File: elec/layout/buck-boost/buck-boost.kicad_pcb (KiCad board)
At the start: 2 copper layers, 62 parts, among them U10 2.49kΩ ±1% 100mW, U11 4.7µF ±10% 100V X7R, U12 4.7µF ±10% 100V X7R, U13 4.7µF ±10% 100V X7R, U14 10µF ±10% 100V X7R, U15 10µF ±10% 100V X7R, U16 10µF ±10% 100V X7R, U17 10µF ±10% 100V X7R, U18 1µF ±10% 100V X7R, U19 100nF ±10% 100V X7R, U2 100nF ±10% 50V X7R, U20 100pF ±5% 100V C0G, U21 470nF ±20% 16V X5R, U22 100nF ±10% 16V X7R, U23 10Ω ±1% 62.5mW, U24 100nF ±10% 16V X7R, U25 10Ω ±1% 62.5mW, U26 5mΩ ±1% 1W, U27 4.7µF ±10% 100V X7R, U28 4.7µF ±10% 100V X7R, U29 4.7µF ±10% 100V X7R, U3 100nF ±10% 50V X7R, U30 10µF ±10% 100V X7R, U31 10µF ±10% 100V X7R, U32 10µF ±10% 100V X7R, U33 10µF ±10% 100V X7R, U34 1µF ±10% 100V X7R, U35 100nF ±10% 100V X7R, U36 100pF ±5% 100V C0G, U37 470nF ±20% 16V X5R, U38 100nF ±10% 16V X7R, U39 10Ω ±1% 62.5mW, U4 0Ω 100mW, U40 100nF ±10% 16V X7R, U41 10Ω ±1% 62.5mW, U42 5mΩ ±1% 1W, U43 13.7kΩ ±1% 62.5mW, U44 249kΩ ±1% 62.5mW, U45 1MΩ ±1% 250mW, U46 133kΩ ±1% 62.5mW, U47 25.5kΩ ±1% 62.5mW, U48 4.7µF ±10% 25V X5R, U49 100nF ±10% 100V X7R, U5 0Ω 100mW, U50 1µF ±10% 100V X7R, U51 4.7µF ±10% 100V X7R, U52 4.7µF ±10% 100V X7R, U6 0Ω 100mW, U7 0Ω 100mW, U9 4.7µF ±10% 25V X5R

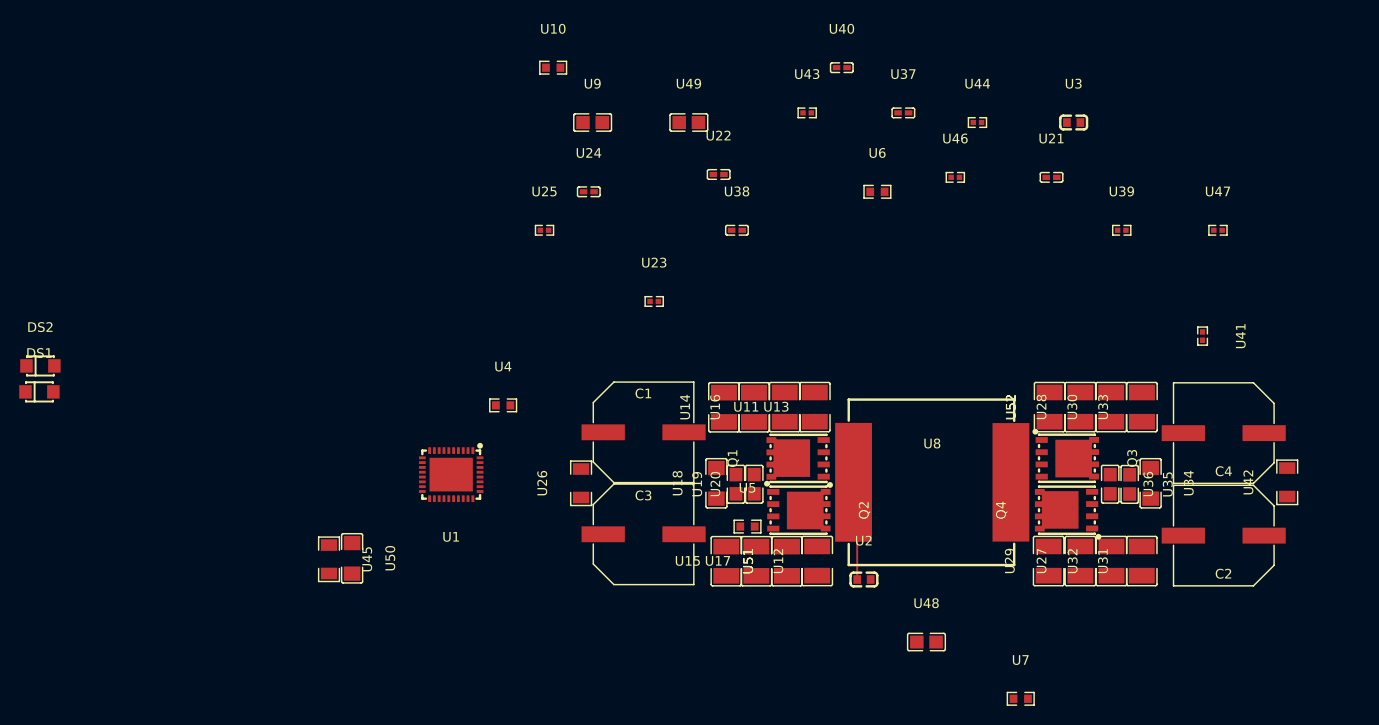
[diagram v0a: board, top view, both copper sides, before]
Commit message: update buck boost
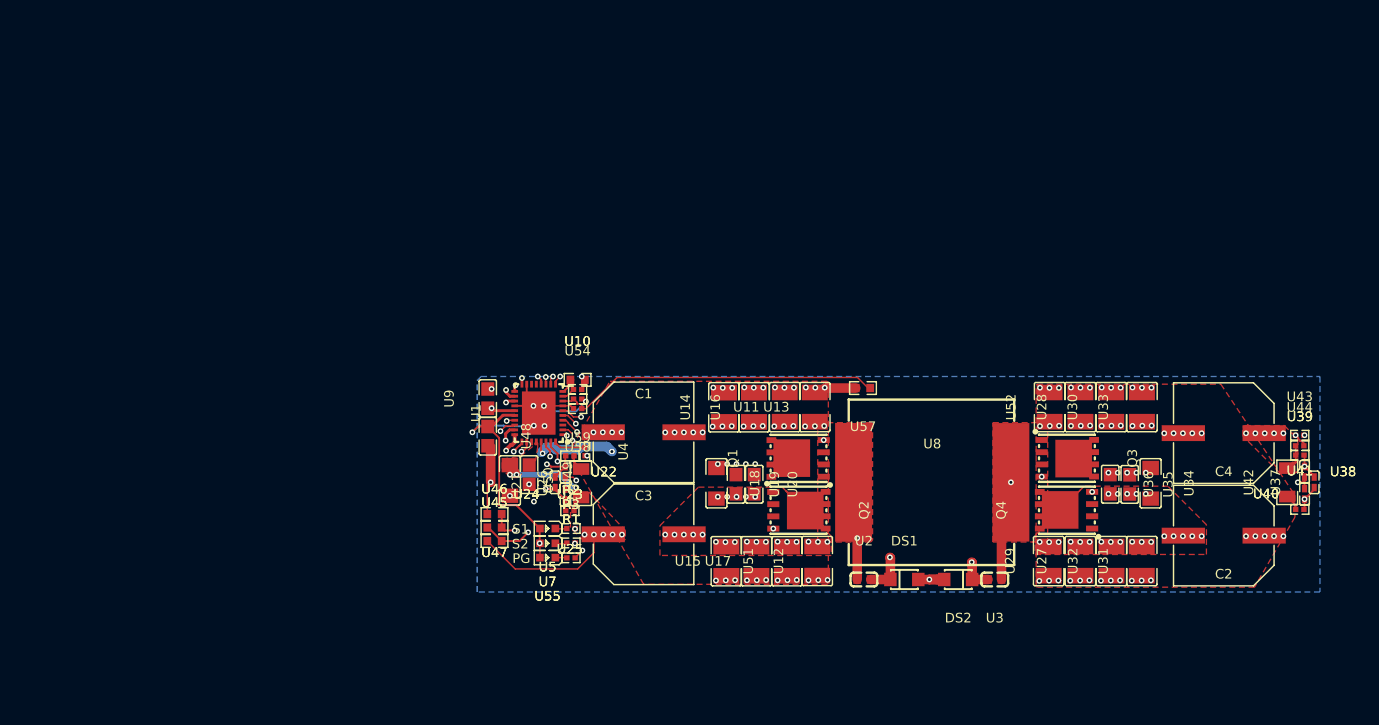
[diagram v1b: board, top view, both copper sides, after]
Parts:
- removed U6: 0Ω 100mW, atopile:R0603-ebcab9
- added R1: 100Ω ±1% 62.5mW, atopile:R0402-56259e, F.Cu at (135.3, 77.2)
- added R2: 100Ω ±1% 62.5mW, atopile:R0402-56259e, F.Cu at (135.3, 74.2)
- added R3: 100Ω ±1% 62.5mW, atopile:R0402-56259e, F.Cu at (135.3, 75.7)
- added U54: 0Ω 62.5mW, atopile:R0402-56259e, F.Cu at (136.0, 59.7)
- added U55: , atopile:LED0603-RD-c81ffb, F.Cu at (132.9, 77.2)
- added U57: , atopile:R0603-ebcab9, F.Cu at (165.7, 59.6)
- added U58: 30.1kΩ ±1% 62.5mW, atopile:R0402-56259e, F.Cu at (136.0, 61.7)
- added U59: 5.23kΩ ±1% 62.5mW, atopile:R0402-56259e, F.Cu at (136.0, 60.7)
- U4: value 0Ω 100mW -> 50kΩ ±1% 62.5mW; footprint atopile:R0603-ebcab9 -> atopile:R0402-56259e
- U45: value 1MΩ ±1% 250mW -> 1MΩ ±1% 100mW; footprint atopile:R1206-bdb864 -> atopile:R0603-ebcab9
- U46: value 133kΩ ±1% 62.5mW -> 133kΩ ±1% 100mW; footprint atopile:R0402-56259e -> atopile:R0603-ebcab9
- U47: value 25.5kΩ ±1% 62.5mW -> 25.5kΩ ±0% 100mW; footprint atopile:R0402-56259e -> atopile:R0603-ebcab9
- U5, U7: value 0Ω 100mW -> (none); footprint atopile:R0603-ebcab9 -> atopile:LED0603-RD-c81ffb
- moved DS2 97.9 mm to (175.6, 79.5), turned to 180 degrees
- moved DS1 92.0 mm to (170.0, 79.5)
- moved U47 80.8 mm to (127.4, 72.7), turned to 180 degrees
- moved U40 65.4 mm to (211.6, 70.6), turned to 90 degrees
- moved U38 64.1 mm to (211.6, 68.3), turned to -90 degrees
- moved U43 61.2 mm to (211.1, 64.5)
- moved U21 60.6 mm to (133.7, 69.4), turned to 90 degrees
- moved U46 60.2 mm to (127.4, 74.1)
- moved U37 57.4 mm to (212.6, 69.4), turned to 90 degrees
- moved U7 51.8 mm to (132.9, 75.7), turned to 180 degrees
- moved U48 50.4 mm to (126.7, 64.6), turned to -90 degrees
- moved U3 48.2 mm to (179.4, 79.5), turned to 180 degrees
- moved U44 47.4 mm to (211.1, 65.6)
- moved U49 40.2 mm to (131.0, 68.6), turned to -90 degrees
- moved U22 34.8 mm to (134.8, 68.3), turned to -90 degrees
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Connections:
- net out renamed FB
- C1 pad 1: hv-1 -> hv-2
- C1 pad 2: gnd -> gnd-3
- C2 pad 2: core.output_cap-net -> gnd-3
- C3 pad 2: gnd -> gnd-3
- C4 pad 1: hv-2 -> hv-1
- C4 pad 2: output_electrolytic-net -> gnd-3
- DS1 pad 1: bst_diode_input.footprint.pins[0].net-net -> cathode-1
- DS1 pad 2: bst_diode_input.footprint.pins[1].net-net -> anode
- DS2 pad 1: bst_diode_output.footprint.pins[0].net-net -> cathode
- DS2 pad 2: bst_diode_output.footprint.pins[1].net-net -> anode
- Q1 pad 1: input_switching_node -> SW1
- Q1 pad 2: input_switching_node -> SW1
- Q1 pad 3: input_switching_node -> SW1
- Q1 pad 4: core-gate-2 -> line-4
- Q1 pad 5: hv-1 -> hv-2
- Q1 pad 6: hv-1 -> hv-2
- Q1 pad 7: hv-1 -> hv-2
- Q1 pad 8: hv-1 -> hv-2
- Q2 pad 1: gnd -> gnd-3
- Q2 pad 2: gnd -> gnd-3
- Q2 pad 3: gnd -> gnd-3
- Q2 pad 4: core-gate -> line-3
- Q2 pad 5: input_switching_node -> SW1
- Q2 pad 6: input_switching_node -> SW1
- Q2 pad 7: input_switching_node -> SW1
- Q2 pad 8: input_switching_node -> SW1
- Q3 pad 1: output_switching_node -> SW2
- Q3 pad 2: output_switching_node -> SW2
- Q3 pad 3: output_switching_node -> SW2
- Q3 pad 4: core-gate-3 -> line
- Q4 pad 1: gnd -> gnd-3
- Q4 pad 2: gnd -> gnd-3
- Q4 pad 3: gnd -> gnd-3
- Q4 pad 4: core-gate-1 -> line-2
- Q4 pad 5: output_switching_node -> SW2
- Q4 pad 6: output_switching_node -> SW2
- Q4 pad 7: output_switching_node -> SW2
- Q4 pad 8: output_switching_node -> SW2
- U1 pad 13: SRN -> output_shunt.diff_cap-net-1
- U1 pad 14: SRP -> output_shunt.diff_cap-net
- U1 pad 17: gnd -> gnd-3
- U1 pad 19: gate_output_hs -> line
- U1 pad 20: anode -> cathode
- U1 pad 21: gate_output_ls -> line-2
- U1 pad 22: gnd -> gnd-3
- U1 pad 24: REGN -> anode-1
- U1 pad 25: gate_input_ls -> line-3
- U1 pad 26: bst_input -> cathode-1
- U1 pad 27: gate_input_hs -> line-4
- U1 pad 29: ACN -> line-7
- U1 pad 30: ACP -> line-5
- U1 pad 33: hv-2 -> hv-1
- U1 pad 37: gnd -> gnd-3
- U1 pad 4: STAT1 -> gnd
- U1 pad 5: STAT2 -> gnd-4
- U1 pad 6: PGh -> gnd-5
- U1 pad 7: CEh -> gnd-3
- U10 pad 2: gnd -> gnd-3
- U11 pad 1: hv-1 -> hv-2
- U11 pad 2: gnd -> gnd-3
- U12 pad 1: hv-1 -> hv-2
- U12 pad 2: gnd -> gnd-3
- U13 pad 1: hv-1 -> hv-2
- U13 pad 2: gnd -> gnd-3
- U14 pad 1: hv-1 -> hv-2
- U14 pad 2: gnd -> gnd-3
- U15 pad 1: hv-1 -> hv-2
- U15 pad 2: gnd -> gnd-3
- U16 pad 1: hv-1 -> hv-2
- U16 pad 2: gnd -> gnd-3
- U17 pad 1: hv-1 -> hv-2
- U17 pad 2: gnd -> gnd-3
- U18 pad 1: hv-1 -> hv-2
- U18 pad 2: gnd -> gnd-3
- U19 pad 1: hv-1 -> hv-2
- U19 pad 2: gnd -> gnd-3
- U2 pad 1: input_switching_node -> SW1
- U2 pad 2: bst_input -> cathode-1
- U20 pad 1: hv-1 -> hv-2
- U20 pad 2: gnd -> gnd-3
- U21 pad 1: input_shunt.diff_cap-net-1 -> line-5
- U21 pad 2: input_shunt.diff_cap-net -> line-7
- U22 pad 1: ACN -> line-7
- U22 pad 2: gnd -> gnd-3
- U23 pad 1: hv-1 -> hv-2
- U23 pad 2: ACN -> line-7
- U24 pad 1: ACP -> line-5
- U24 pad 2: gnd -> gnd-3
- U25 pad 2: ACP -> line-5
- U26 pad 2: hv-1 -> hv-2
- U27 pad 2: gnd -> gnd-3
- U28 pad 2: gnd -> gnd-3
- U29 pad 2: gnd -> gnd-3
- U3 pad 1: output_switching_node -> SW2
- U3 pad 2: anode -> cathode
- U30 pad 2: gnd -> gnd-3
- U31 pad 2: gnd -> gnd-3
- U32 pad 2: gnd -> gnd-3
- U33 pad 2: gnd -> gnd-3
- U34 pad 2: gnd -> gnd-3
- U35 pad 2: gnd -> gnd-3
- U36 pad 2: gnd -> gnd-3
- U37 pad 1: output_shunt.diff_cap-net-1 -> output_shunt.diff_cap-net
- U37 pad 2: output_shunt.diff_cap-net -> output_shunt.diff_cap-net-1
- U38 pad 1: SRN -> output_shunt.diff_cap-net-1
- U38 pad 2: gnd -> gnd-3
- U39 pad 1: hv-2 -> hv-1
- U39 pad 2: SRN -> output_shunt.diff_cap-net-1
- U4 pad 1: gate_input_hs -> FSW_SYNC
- U4 pad 2: core-gate-2 -> gnd-3
- U40 pad 1: SRP -> output_shunt.diff_cap-net
- U40 pad 2: gnd -> gnd-3
- U41 pad 2: SRP -> output_shunt.diff_cap-net
- U42 pad 2: hv-2 -> hv-1
- U44 pad 1: hv-2 -> hv-1
- U47 pad 2: gnd -> gnd-3
- U48 pad 1: REGN -> anode-1
- U48 pad 2: gnd -> gnd-3
- U49 pad 2: gnd -> gnd-3
- U5 pad 1: gate_input_ls -> status_1_led-cathode
- U5 pad 2: core-gate -> anode-1
- U50 pad 2: gnd -> gnd-3
- U51 pad 1: hv-1 -> hv-2
- U51 pad 2: gnd -> gnd-3
- U52 pad 2: gnd -> gnd-3
- U7 pad 1: gate_output_ls -> status_2_led-cathode
- U7 pad 2: core-gate-1 -> anode-1
- U8 pad 1: input_switching_node -> SW1
- U8 pad 2: output_switching_node -> SW2
- U9 pad 2: gnd -> gnd-3
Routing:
- net output_shunt.diff_cap-net: track 0.00 -> 88.9 mm, vias 0 -> 2
- net output_shunt.diff_cap-net-1: track 0.00 -> 86.4 mm, vias 0 -> 2
- net FB: track 0.00 -> 82.8 mm, vias 0 -> 2
- net gnd-1: track 0.00 -> 81.7 mm, vias 0 -> 2
- net hv-1: track 0.00 -> 78.8 mm, vias 0 -> 7
- net anode: track 0.00 -> 70.3 mm, vias 0 -> 2
- net SW2: track 0.00 -> 68.3 mm, vias 0 -> 2
- net line-2: track 0.00 -> 67.3 mm, vias 0 -> 2
- net cathode: track 0.00 -> 62.4 mm, vias 0 -> 2
- net cathode-1: track 0.00 -> 59.5 mm, vias 0 -> 2
- net line: track 0.00 -> 59.3 mm, vias 0 -> 2
- net SW1: track 0.00 -> 55.2 mm, vias 0 -> 3
- net line-3: track 0.00 -> 38.0 mm, vias 0 -> 2
- net line-4: track 0.00 -> 37.8 mm, vias 0 -> 2
- net anode-1: track 0.00 -> 35.4 mm, vias 0 -> 3
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- added copper zone on F.Cu, net SW1
- added copper zone on F.Cu, net SW2
- added copper zone on B.Cu, net gnd-3
- added copper zone on F.Cu, net gnd-3
- added copper zone on In1.Cu, net gnd-3
- added copper zone on F.Cu, net hv
- added copper zone on F.Cu, net hv-1
- added copper zone on F.Cu, net hv-2
- added copper zone on In2.Cu, net hv-2
- added copper zone on F.Cu, net hv-3
- added copper zone on In2.Cu, net hv-3
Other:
- copper layers 2 -> 6
- board text added: "PG"
- board text added: "S1"
- board text added: "S2"

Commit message: Everything builds
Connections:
- net SW1 renamed core-line
- net SW2 renamed source
- net line-2 renamed gate
- net line-4 renamed gate-1
- net line-7 renamed input_shunt.diff_cap-net
- net output_shunt.diff_cap-net renamed line-1
- C1 pad 2: gnd-3 -> gnd-4
- C2 pad 1: hv-3 -> hv
- C2 pad 2: gnd-3 -> gnd-4
- C3 pad 1: hv -> hv-3
- C3 pad 2: gnd-3 -> gnd-4
- C4 pad 2: gnd-3 -> gnd-4
- DS1 pad 1: cathode-1 -> cathode
- DS2 pad 1: cathode -> cathode-1
- Q2 pad 1: gnd-3 -> gnd-4
- Q2 pad 2: gnd-3 -> gnd-4
- Q2 pad 3: gnd-3 -> gnd-4
- Q2 pad 4: line-3 -> gate-2
- Q3 pad 5: hv-3 -> hv
- Q3 pad 6: hv-3 -> hv
- Q3 pad 7: hv-3 -> hv
- Q3 pad 8: hv-3 -> hv
- Q4 pad 1: gnd-3 -> gnd-4
- Q4 pad 2: gnd-3 -> gnd-4
- Q4 pad 3: gnd-3 -> gnd-4
- R1 pad 2: gnd-5 -> gnd-6
- R2 pad 2: gnd -> gnd-1
- R3 pad 2: gnd-4 -> gnd-3
- U1 pad 11: gnd-1 -> gnd-5
- U1 pad 17: gnd-3 -> gnd-4
- U1 pad 20: cathode -> cathode-1
- U1 pad 22: gnd-3 -> gnd-4
- U1 pad 25: line-3 -> gate-2
- U1 pad 26: cathode-1 -> cathode
- U1 pad 30: line-5 -> line-3
- U1 pad 32: hv -> hv-3
- U1 pad 37: gnd-3 -> gnd-4
- U1 pad 4: gnd -> gnd-1
- U1 pad 5: gnd-4 -> gnd-3
- U1 pad 6: gnd-5 -> gnd-6
- U1 pad 7: gnd-3 -> gnd-4
- U10 pad 2: gnd-3 -> gnd-4
- U11 pad 2: gnd-3 -> gnd-4
- U12 pad 2: gnd-3 -> gnd-4
- U13 pad 2: gnd-3 -> gnd-4
- U14 pad 2: gnd-3 -> gnd-4
- U15 pad 2: gnd-3 -> gnd-4
- U16 pad 2: gnd-3 -> gnd-4
- U17 pad 2: gnd-3 -> gnd-4
- U18 pad 2: gnd-3 -> gnd-4
- U19 pad 2: gnd-3 -> gnd-4
- U2 pad 2: cathode-1 -> cathode
- U20 pad 2: gnd-3 -> gnd-4
- U21 pad 1: line-5 -> line-3
- U22 pad 2: gnd-3 -> gnd-4
- U24 pad 1: line-5 -> line-3
- U24 pad 2: gnd-3 -> gnd-4
- U25 pad 1: hv -> hv-3
- U25 pad 2: line-5 -> line-3
- U26 pad 1: hv -> hv-3
- U27 pad 1: hv-3 -> hv
- U27 pad 2: gnd-3 -> gnd-4
- U28 pad 1: hv-3 -> hv
- U28 pad 2: gnd-3 -> gnd-4
- U29 pad 1: hv-3 -> hv
- U29 pad 2: gnd-3 -> gnd-4
- U3 pad 2: cathode -> cathode-1
- U30 pad 1: hv-3 -> hv
- U30 pad 2: gnd-3 -> gnd-4
- U31 pad 1: hv-3 -> hv
- U31 pad 2: gnd-3 -> gnd-4
- U32 pad 1: hv-3 -> hv
- U32 pad 2: gnd-3 -> gnd-4
- U33 pad 1: hv-3 -> hv
- U33 pad 2: gnd-3 -> gnd-4
- U34 pad 1: hv-3 -> hv
- U34 pad 2: gnd-3 -> gnd-4
- U35 pad 1: hv-3 -> hv
- U35 pad 2: gnd-3 -> gnd-4
- U36 pad 1: hv-3 -> hv
- U36 pad 2: gnd-3 -> gnd-4
- U38 pad 2: gnd-3 -> gnd-4
- U4 pad 2: gnd-3 -> gnd-4
- U40 pad 2: gnd-3 -> gnd-4
- U41 pad 1: hv-3 -> hv
- U42 pad 1: hv-3 -> hv
- U43 pad 2: gnd-1 -> gnd-5
- U45 pad 1: hv -> hv-3
- U47 pad 2: gnd-3 -> gnd-4
- U48 pad 2: gnd-3 -> gnd-4
- U49 pad 1: hv -> hv-3
- U49 pad 2: gnd-3 -> gnd-4
- U50 pad 1: hv -> hv-3
- U50 pad 2: gnd-3 -> gnd-4
- U51 pad 2: gnd-3 -> gnd-4
- U52 pad 1: hv-3 -> hv
- U52 pad 2: gnd-3 -> gnd-4
- U54 pad 2: gnd-3 -> gnd-4
- U57 pad 2: gnd-3 -> gnd-4
- U58 pad 2: gnd-3 -> gnd-4
- U9 pad 2: gnd-3 -> gnd-4
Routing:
- net gnd-1: track 81.7 -> 12.5 mm
- net gnd-5: track 17.4 -> 81.7 mm
- net gate-2: track 0.00 -> 38.0 mm, vias 0 -> 2
- net line-3: track 38.0 -> 10.1 mm
- net hv-3: track 1.69 -> 27.9 mm, vias 34 -> 8
- net hv: track 27.9 -> 1.69 mm, vias 8 -> 34
- net gnd-6: track 0.00 -> 17.4 mm, vias 0 -> 2
- net gnd: track 12.5 -> 0.00 mm, vias 2 -> 0
- net line-5: track 10.1 -> 0.00 mm, vias 2 -> 0
- net gnd-4: track 15.6 -> 24.6 mm, vias 2 -> 90
- net gnd-3: track 24.6 -> 15.6 mm, vias 90 -> 2
- net cathode-1: track 59.5 -> 62.4 mm
- net cathode: track 62.4 -> 59.5 mm
- added copper zone on B.Cu, net gnd-4
- added copper zone on F.Cu, net gnd-4
- added copper zone on In1.Cu, net gnd-4
- added copper zone on In2.Cu, net hv
- removed copper zone on B.Cu, net gnd-3
- removed copper zone on F.Cu, net gnd-3
- removed copper zone on In1.Cu, net gnd-3
- removed copper zone on In2.Cu, net hv-3

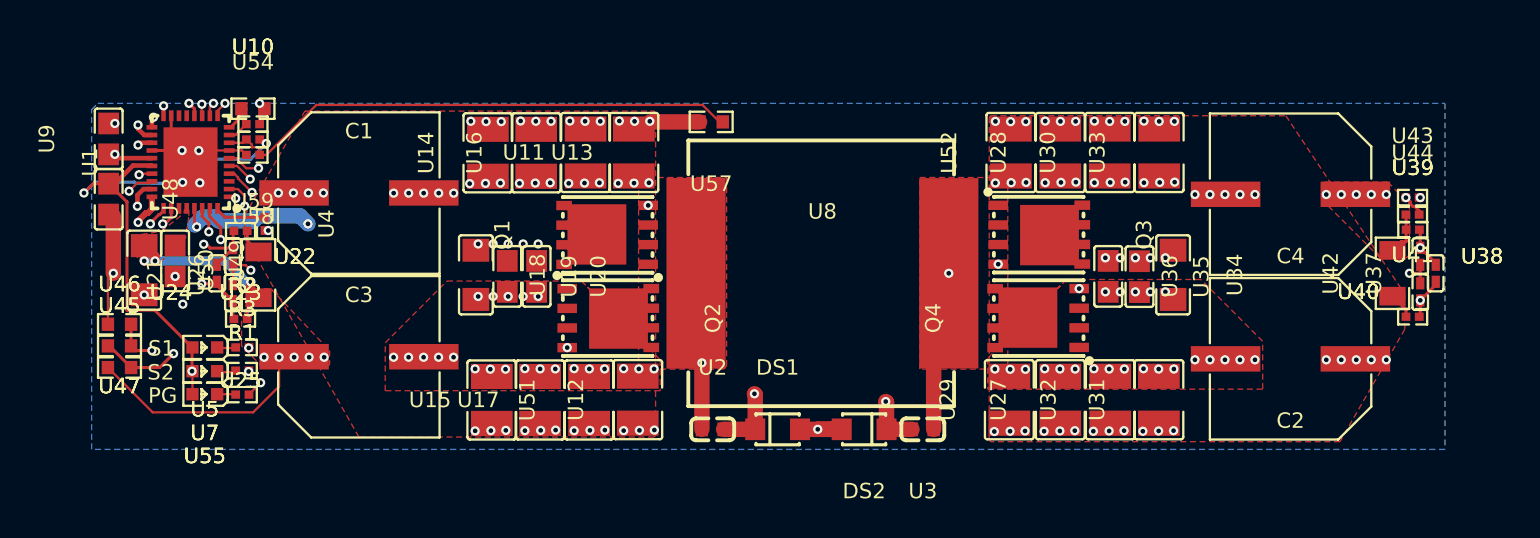
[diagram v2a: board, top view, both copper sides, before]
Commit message: connect core gnd to input power gnd
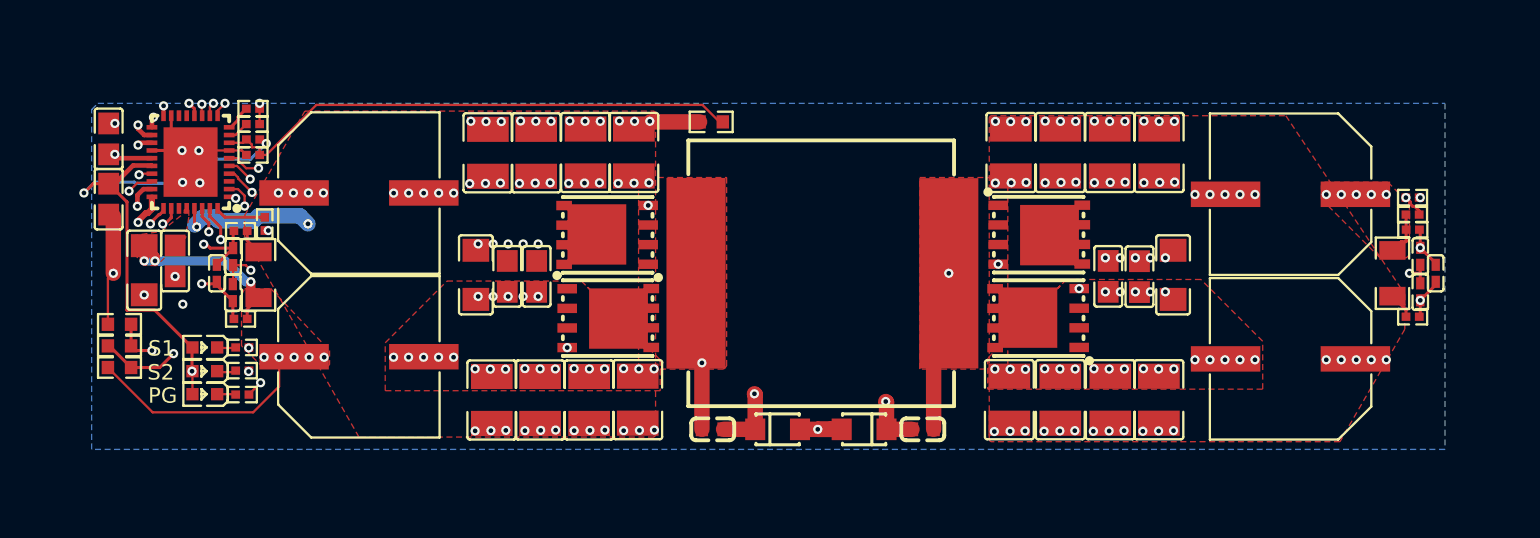
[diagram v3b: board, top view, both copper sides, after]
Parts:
- C1, C2, C3, C4: value 68µF ±20% infV -> 68µF ±20%
- U10: value 2.49kΩ ±1% 100mW -> 2.49kΩ ±1% 62.5mW; footprint atopile:R0603-ebcab9 -> atopile:R0402-56259e
- U44: value 249kΩ ±1% 62.5mW -> 249kΩ ±0%
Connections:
- net core-line renamed line-2
- net gate-2 renamed line-6
- net input_shunt.diff_cap-net renamed line-4
- net source renamed drain
- C1 pad 1: hv-2 -> hv-1
- C1 pad 2: gnd-4 -> gnd
- C2 pad 2: gnd-4 -> gnd
- C3 pad 2: gnd-4 -> gnd
- C4 pad 1: hv-1 -> hv-2
- C4 pad 2: gnd-4 -> gnd
- DS1 pad 1: cathode -> cathode-1
- DS2 pad 1: cathode-1 -> cathode
- Q1 pad 4: gate-1 -> line-3
- Q1 pad 5: hv-2 -> hv-1
- Q1 pad 6: hv-2 -> hv-1
- Q1 pad 7: hv-2 -> hv-1
- Q1 pad 8: hv-2 -> hv-1
- Q2 pad 1: gnd-4 -> gnd
- Q2 pad 2: gnd-4 -> gnd
- Q2 pad 3: gnd-4 -> gnd
- Q3 pad 4: line -> gate
- Q4 pad 1: gnd-4 -> gnd
- Q4 pad 2: gnd-4 -> gnd
- Q4 pad 3: gnd-4 -> gnd
- Q4 pad 4: gate -> gate-1
- R1 pad 2: gnd-6 -> gnd-4
- R2 pad 2: gnd-1 -> gnd-3
- R3 pad 2: gnd-3 -> gnd-2
- U1 pad 11: gnd-5 -> gnd-1
- U1 pad 13: output_shunt.diff_cap-net-1 -> line
- U1 pad 17: gnd-4 -> gnd
- U1 pad 19: line -> gate
- U1 pad 20: cathode-1 -> cathode
- U1 pad 21: gate -> gate-1
- U1 pad 22: gnd-4 -> gnd
- U1 pad 26: cathode -> cathode-1
- U1 pad 27: gate-1 -> line-3
- U1 pad 30: line-3 -> line-5
- U1 pad 33: hv-1 -> hv-2
- U1 pad 37: gnd-4 -> gnd
- U1 pad 4: gnd-1 -> gnd-3
- U1 pad 5: gnd-3 -> gnd-2
- U1 pad 6: gnd-6 -> gnd-4
- U1 pad 7: gnd-4 -> gnd
- U10 pad 2: gnd-4 -> gnd
- U11 pad 1: hv-2 -> hv-1
- U11 pad 2: gnd-4 -> gnd
- U12 pad 1: hv-2 -> hv-1
- U12 pad 2: gnd-4 -> gnd
- U13 pad 1: hv-2 -> hv-1
- U13 pad 2: gnd-4 -> gnd
- U14 pad 1: hv-2 -> hv-1
- U14 pad 2: gnd-4 -> gnd
- U15 pad 1: hv-2 -> hv-1
- U15 pad 2: gnd-4 -> gnd
- U16 pad 1: hv-2 -> hv-1
- U16 pad 2: gnd-4 -> gnd
- U17 pad 1: hv-2 -> hv-1
- U17 pad 2: gnd-4 -> gnd
- U18 pad 1: hv-2 -> hv-1
- U18 pad 2: gnd-4 -> gnd
- U19 pad 1: hv-2 -> hv-1
- U19 pad 2: gnd-4 -> gnd
- U2 pad 2: cathode -> cathode-1
- U20 pad 1: hv-2 -> hv-1
- U20 pad 2: gnd-4 -> gnd
- U21 pad 1: line-3 -> line-5
- U22 pad 2: gnd-4 -> gnd
- U23 pad 1: hv-2 -> hv-1
- U24 pad 1: line-3 -> line-5
- U24 pad 2: gnd-4 -> gnd
- U25 pad 2: line-3 -> line-5
- U26 pad 2: hv-2 -> hv-1
- U27 pad 2: gnd-4 -> gnd
- U28 pad 2: gnd-4 -> gnd
- U29 pad 2: gnd-4 -> gnd
- U3 pad 2: cathode-1 -> cathode
- U30 pad 2: gnd-4 -> gnd
- U31 pad 2: gnd-4 -> gnd
- U32 pad 2: gnd-4 -> gnd
- U33 pad 2: gnd-4 -> gnd
- U34 pad 2: gnd-4 -> gnd
- U35 pad 2: gnd-4 -> gnd
- U36 pad 2: gnd-4 -> gnd
- U37 pad 2: output_shunt.diff_cap-net-1 -> line
- U38 pad 1: output_shunt.diff_cap-net-1 -> line
- U38 pad 2: gnd-4 -> gnd
- U39 pad 1: hv-1 -> hv-2
- U39 pad 2: output_shunt.diff_cap-net-1 -> line
- U4 pad 2: gnd-4 -> gnd
- U40 pad 2: gnd-4 -> gnd
- U42 pad 2: hv-1 -> hv-2
- U43 pad 2: gnd-5 -> gnd-1
- U44 pad 1: hv-1 -> hv-2
- U47 pad 2: gnd-4 -> gnd
- U48 pad 2: gnd-4 -> gnd
- U49 pad 2: gnd-4 -> gnd
- U50 pad 2: gnd-4 -> gnd
- U51 pad 1: hv-2 -> hv-1
- U51 pad 2: gnd-4 -> gnd
- U52 pad 2: gnd-4 -> gnd
- U54 pad 2: gnd-4 -> gnd
- U57 pad 2: gnd-4 -> gnd
- U58 pad 2: gnd-4 -> gnd
- U9 pad 2: gnd-4 -> gnd
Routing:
- net output_shunt.diff_cap-net-1: track 86.4 -> 0.00 mm, vias 2 -> 0
- net gnd-5: track 81.7 -> 0.00 mm, vias 2 -> 0
- net hv-2: track 1.67 -> 78.8 mm, vias 33 -> 7
- net hv-1: track 78.8 -> 1.67 mm, vias 7 -> 33
- net gnd-1: track 12.5 -> 81.7 mm
- net gate-1: track 37.8 -> 67.3 mm
- net line-3: track 10.1 -> 37.8 mm
- net line: track 59.3 -> 86.4 mm
- net gnd: track 0.00 -> 24.6 mm, vias 0 -> 90
- net gnd-6: track 17.4 -> 0.00 mm, vias 2 -> 0
- net gnd-2: track 0.00 -> 15.6 mm, vias 0 -> 2
- net SDA: track 14.0 -> 1.85 mm
- net SCL: track 11.2 -> 0.46 mm
- net line-5: track 0.00 -> 10.1 mm, vias 0 -> 2
- net gate: track 67.3 -> 59.3 mm
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- added copper zone on B.Cu, net gnd
- added copper zone on F.Cu, net gnd
- added copper zone on In1.Cu, net gnd
- added copper zone on In2.Cu, net hv-1
- removed copper zone on B.Cu, net gnd-4
- removed copper zone on F.Cu, net gnd-4
- removed copper zone on In1.Cu, net gnd-4
- removed copper zone on In2.Cu, net hv-2
